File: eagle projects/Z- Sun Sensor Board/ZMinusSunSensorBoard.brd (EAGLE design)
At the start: 91 x 91 mm, 204 parts, among them J1 TE-1734829-2, U1 ADS7841E_2K5, U10 TSV991AILT, U11 TSV991AILT, U12 TSV991AILT, U13 ADS7841E_2K5, U14 TSV991AILT, U16 TSV991AILT, U17 TSV991AILT, U19 TSV991AILT, U2 ADS7841E_2K5, U21 TSV991AILT, U23 TSV991AILT, U25 ADS7841E_2K5, U26 TSV991AILT, U27 ADS7841E_2K5, U29 TSV991AILT, U3 TSV991AILT, U4 LM20BIM7X_NOPB, U5 LM20BIM7X_NOPB, U6 TSV991AILT, U8 TSV991AILT, U9 TSV991AILT

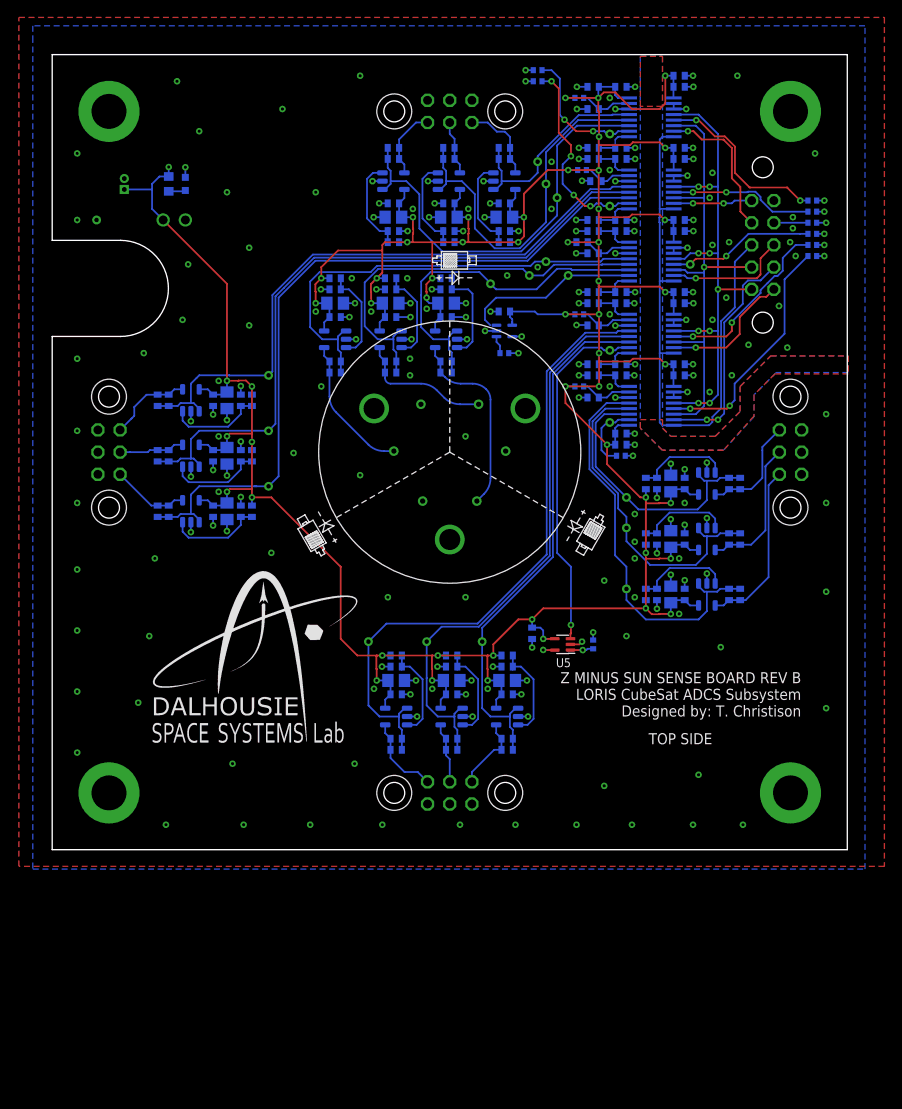
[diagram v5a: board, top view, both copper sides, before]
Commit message: Changed most connector changes of Z- board
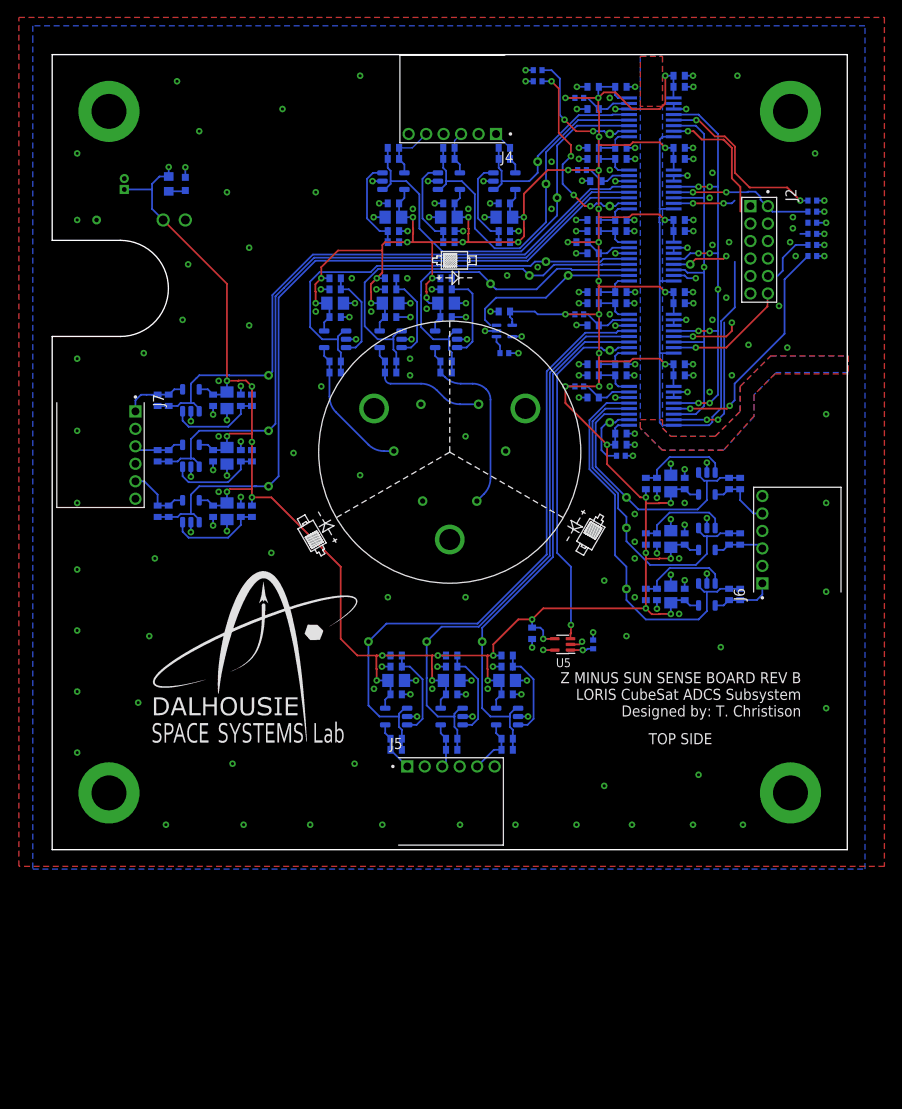
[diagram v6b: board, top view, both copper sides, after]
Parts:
- removed JP2, JP4, JP5, JP6: (no value), my_library:2X03_MTG_HOLES
- added J4, J5, J6, J7: 830-10-006-20-005000, 830-10-006-20-005000:830-10-006-20-005000
- J2: value (none) -> 832-10-012-10-005000; device my_library:2X05 -> 832-10-012-10-005000:832-10-012-10-005000
- moved J2 4.48 mm to (81.9, 73.7), flipped to the top, turned to 270 degrees
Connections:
- removed net N$23: C96.1, JP6.4, R75.1, U26.4
- removed net N$35: C103.1, JP6.2, R81.1, U29.4
- removed net N$37: C34.1, JP5.2, R45.1, U12.4
- removed net N$63: C59.1, JP5.4, R52.1, U19.4
- new net N$13: C96.1, J7.3, R75.1, U26.4
- new net N$17: C103.1, J7.5, R81.1, U29.4
- new net N$3: C34.1, J6.5, R45.1, U12.4
- new net N$5: C59.1, J6.3, R52.1, U19.4
- net !CS!_SUN_X+: now also J2.12; no longer J2.2
- net !CS!_SUN_X-: now also J2.5; no longer J2.7
- net !CS!_SUN_Y+: now also J2.10; no longer J2.4
- net !CS!_SUN_Y-: now also J2.3; no longer J2.9
- net !CS!_SUN_Z-: now also J2.8; no longer J2.6
- net +3V3: now also J2.4; no longer J2.10
- net GND: now also J4.2, J4.4, J4.6, J5.2, J5.4, J5.6, J6.2, J6.4, J6.6, J7.2, J7.4, J7.6; no longer JP2.1, JP2.3, JP2.5, JP4.1, JP4.3, JP4.5, JP5.1, JP5.3, JP5.5, JP6.1, JP6.3, JP6.5
- net N$29: now also J7.1; no longer JP6.6
- net N$38: now also J4.5; no longer JP4.2
- net N$44: now also J4.3; no longer JP4.4
- net N$46: now also J4.1; no longer JP4.6
- net N$49: now also J5.5; no longer JP2.2
- net N$55: now also J5.3; no longer JP2.4
- net N$57: now also J5.1; no longer JP2.6
- net N$65: now also J6.1; no longer JP5.6
- net N$67: now also J2.6; no longer J2.8
- net UCB0_SPI_CLK: now also J2.7; no longer J2.5
- net UCB0_SPI_MISO: now also J2.11; no longer J2.1
- net UCB0_SPI_MOSI: now also J2.9; no longer J2.3
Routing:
- net N$63: track 16.3 -> 0.00 mm
- net N$65: track 19.7 -> 7.19 mm
- net N$37: track 12.5 -> 0.00 mm
- net !CS!_SUN_Z-: track 14.3 -> 2.66 mm
- net !CS!_SUN_Y+: track 26.0 -> 16.5 mm
- net N$2: track 16.8 -> 7.29 mm
- net N$35: track 8.89 -> 0.00 mm
- net N$51: track 21.4 -> 13.8 mm
- net N$3: track 0.00 -> 7.56 mm
- net N$17: track 0.00 -> 7.54 mm
- net N$23: track 7.50 -> 0.00 mm
- net N$5: track 0.00 -> 5.83 mm
- net UCB0_SPI_MOSI: track 54.9 -> 49.4 mm
- net N$13: track 0.00 -> 5.22 mm
- net N$46: track 9.41 -> 5.37 mm
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
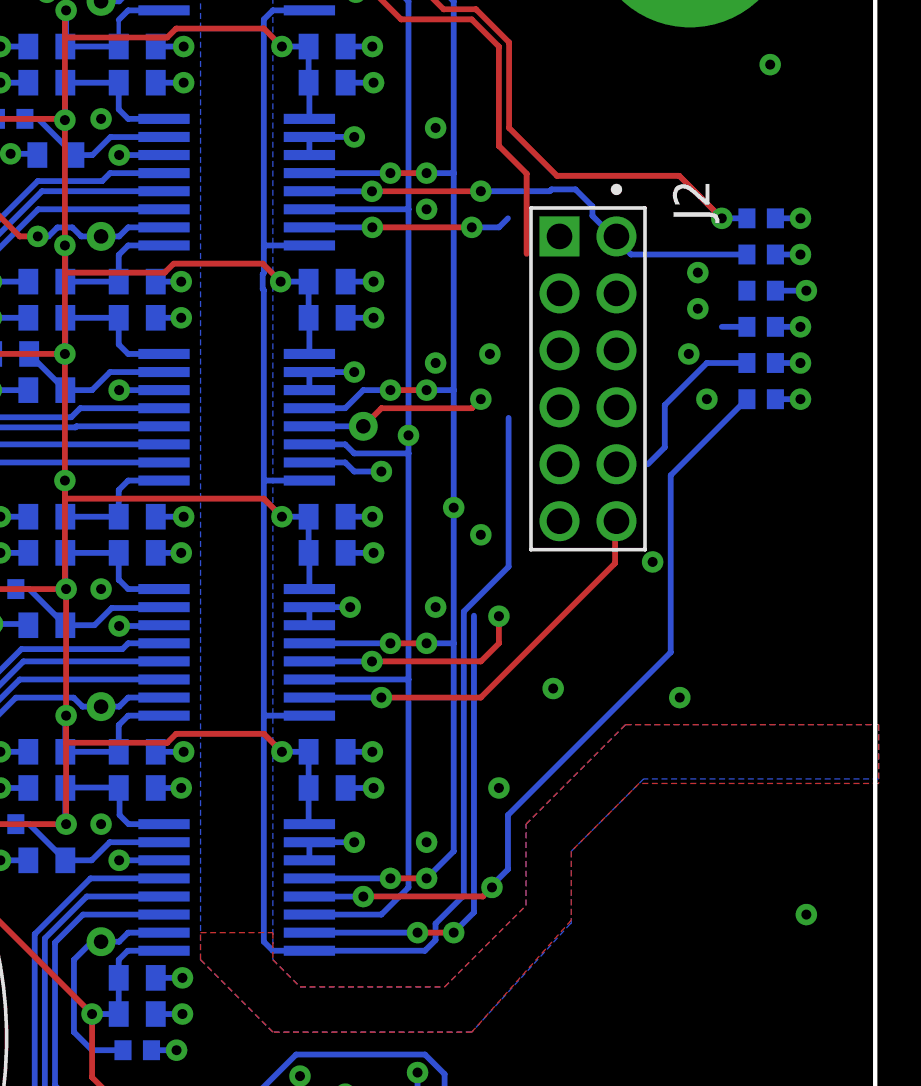
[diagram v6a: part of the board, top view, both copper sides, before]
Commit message: Finished Z- Sun Sensor
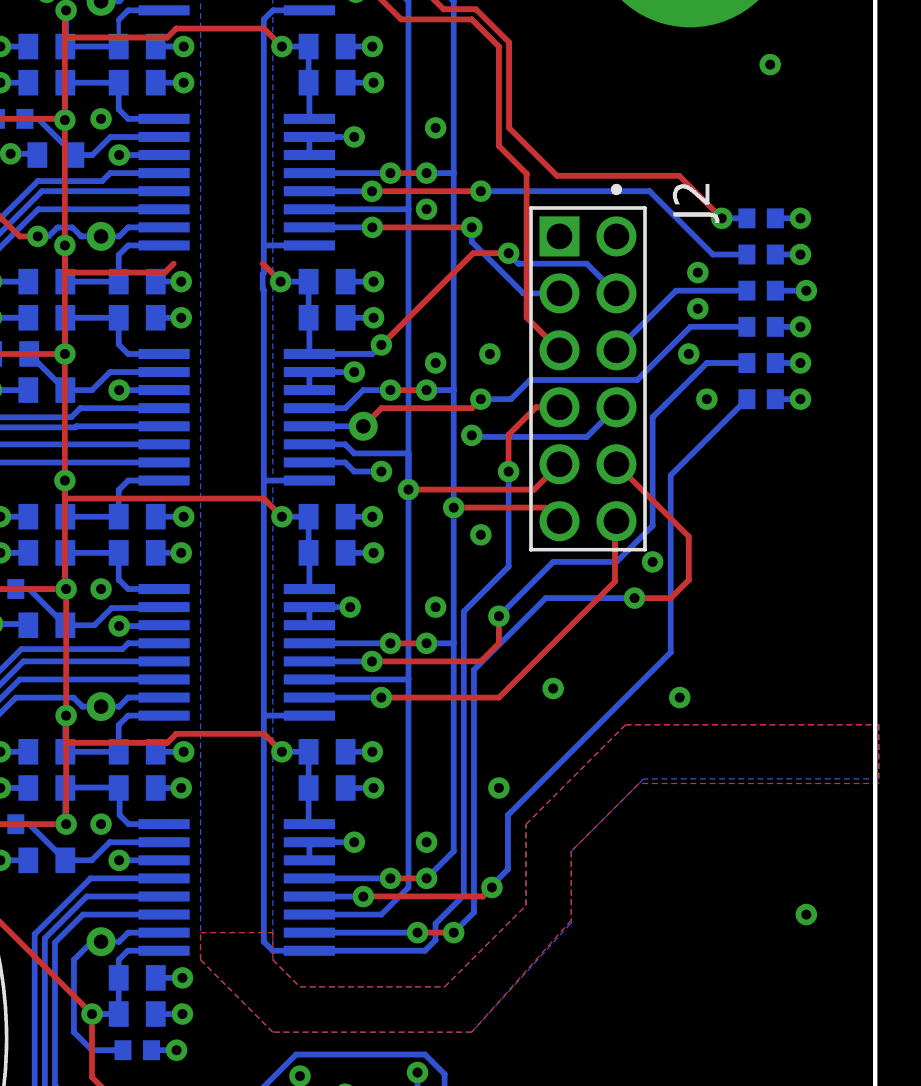
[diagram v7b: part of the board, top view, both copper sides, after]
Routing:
- net !CS!_SUN_Y+: track 16.5 -> 28.6 mm, vias 2 -> 3
- net +3V3: track 497.4 -> 507.1 mm, vias 53 -> 55
- net N$2: track 7.29 -> 16.8 mm
- net N$51: track 13.8 -> 22.6 mm
- net UCB0_SPI_MOSI: track 49.4 -> 56.4 mm
- net !CS!_SUN_Z-: track 2.66 -> 8.19 mm, vias 1 -> 2
- net N$67: track 0.00 -> 5.45 mm
- net UCB0_SPI_MISO: track 56.8 -> 60.7 mm
- net !CS!_SUN_X-: track 15.1 -> 19.0 mm
- net !CS!_SUN_Y-: track 7.10 -> 10.0 mm
- net UCB0_SPI_CLK: track 64.7 -> 66.3 mm, vias 0 -> 1

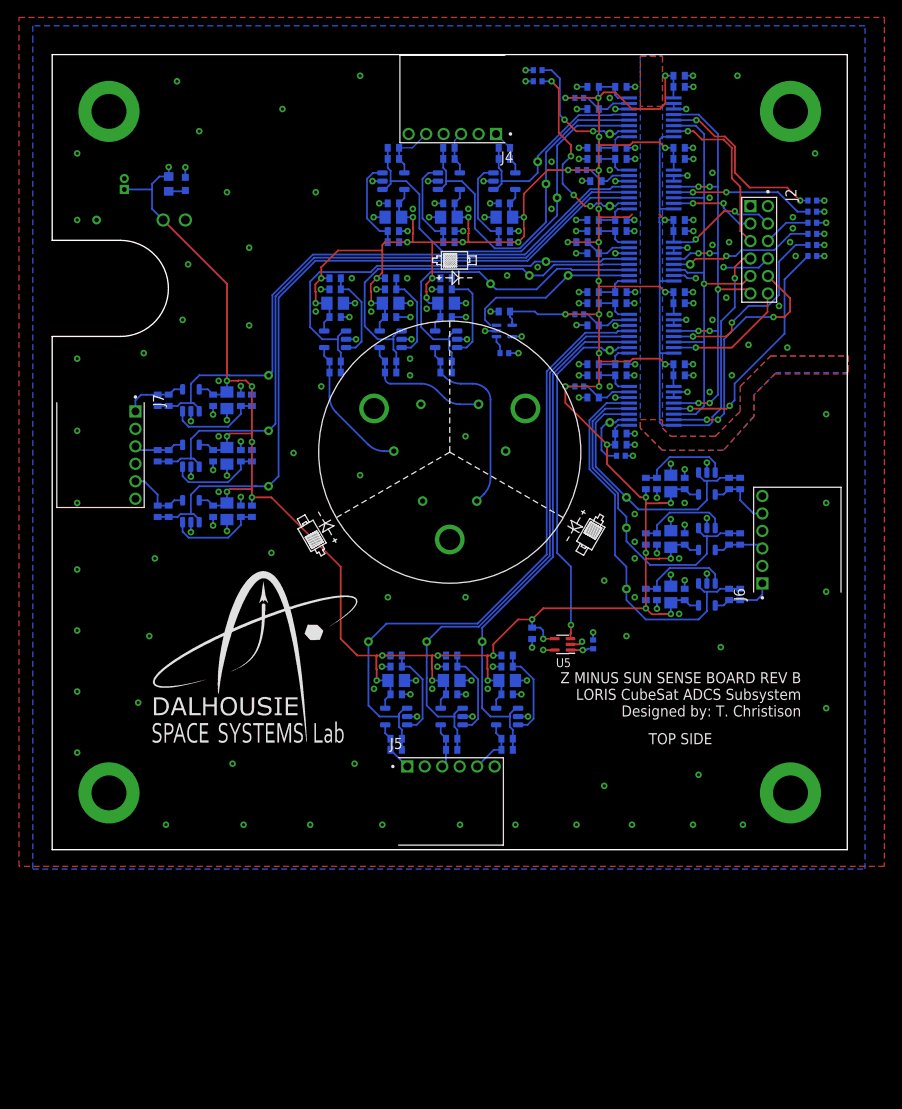
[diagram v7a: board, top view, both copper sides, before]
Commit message: Cleaned up errors in Z+ and Z- boards
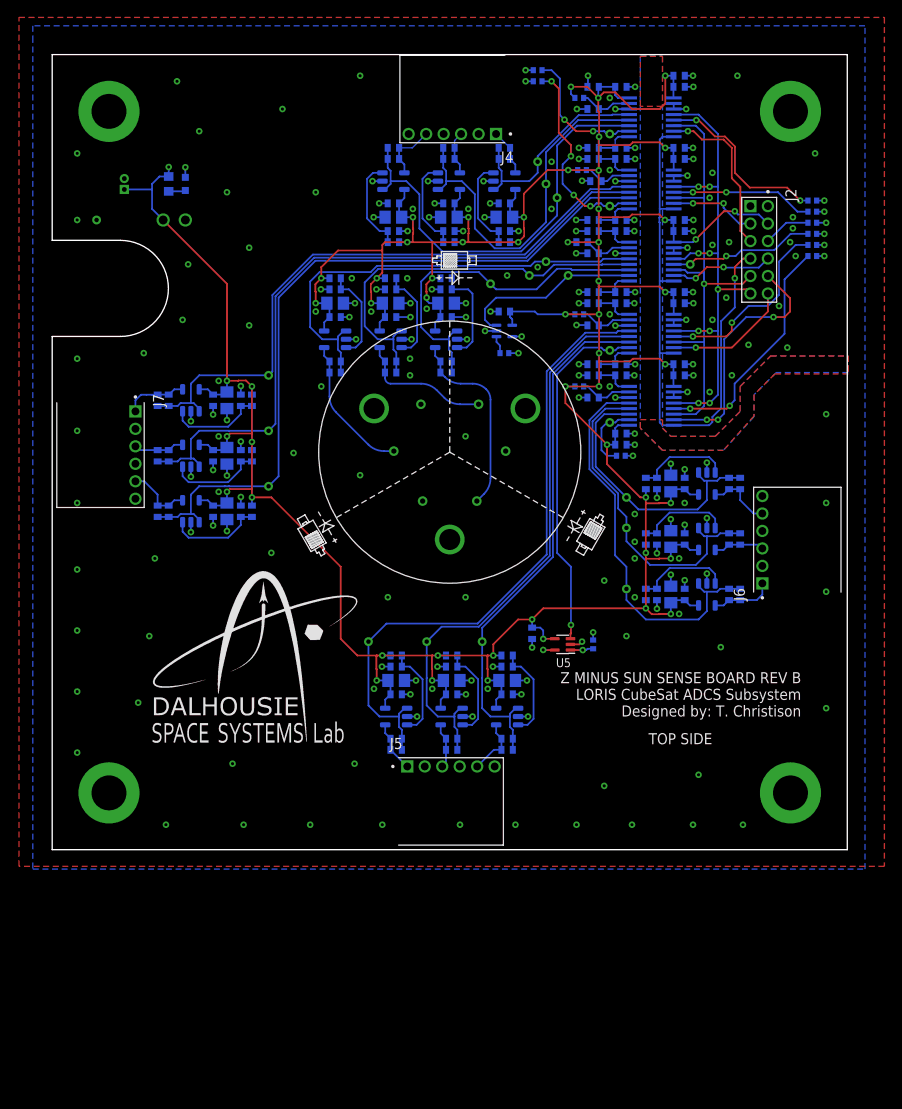
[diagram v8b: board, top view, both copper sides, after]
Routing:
- net !CS!_SUN_Z-: track 8.19 -> 11.9 mm
- net +3V3: track 507.1 -> 510.1 mm
- net TEMP_INT: track 20.2 -> 20.9 mm
- net N$13: track 5.22 -> 5.83 mm
- net GND: track 139.9 -> 140.0 mm, vias 166 -> 220
